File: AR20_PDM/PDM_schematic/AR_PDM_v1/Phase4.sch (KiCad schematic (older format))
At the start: 10 parts, among them Q7 BTS50025-1TAD, U7 INA233

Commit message: Working on pcb layout
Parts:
- removed D?: D_Schottky_x2, symbol AR20_PDM_v1-rescue:D_Schottky_x2
- added D53, D54: D_Schottky_BAT60A, AR_PDM_v1:D_Shotky_BAT60_HandSoldering, symbol AR20_PDM_v1-rescue:D_Schottky_BAT60A
- gave numbers to parts that had none: 4
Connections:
- net GND: now also D53.2 (A), D54.2 (A)
- net at R117.1, U7.10 (IN+): now also D54.1 (K)
- net at R115.1, U7.9 (In-): now also D53.1 (K)
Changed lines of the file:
@@
 AR Path="/5E0FB5C8/5EE91E06" Ref="R?"  Part="1"
 AR Path="/5E0FBBBD/5EE91E06" Ref="R?"  Part="1"
-AR Path="/5E0FC3A2/5EE91E06" Ref="R?"  Part="1"
+AR Path="/5E0FC3A2/5EE91E06" Ref="R116"  Part="1"
 AR Path="/5E0FCFDC/5EE91E06" Ref="R?"  Part="1"
 AR Path="/5E0FDCCC/5EE91E06" Ref="R?"  Part="1"
 AR Path="/5E10174B/5EE91E06" Ref="R?"  Part="1"
-F 0 "R?" V 6643 1600 50  0000 C CNN
+F 0 "R116" V 6643 1600 50  0000 C CNN
 F 1 "2m_1%_4W" V 6734 1600 50  0000 C CNN
 F 2 "Resistor_SMD:R_2512_6332Metric" V 6780 1600 50  0001 C CNN
@@
 Text HLabel 7300 1600 2    50   Input ~ 10
 V+12V
-$Comp
-L AR20_PDM_v1-rescue:D_Schottky_x2 D?
-U 1 1 5EE91E0D
-P 6950 4825
-AR Path="/5DA89415/5EE91E0D" Ref="D?"  Part="1"
-AR Path="/5E0FC3A2/5EE91E0D" Ref="D?"  Part="1"
-F 0 "D?" H 6950 5041 50  0000 C CNN
-F 1 "D_Schottky_x2" H 6950 4950 50  0000 C CNN
-F 2 "" H 6950 4825 50  0001 C CNN
-F 3 "~" H 6950 4825 50  0001 C CNN
-	1    6950 4825
-	1    0    0    -1
-$EndComp
 $Comp
 L AR20_PDM_v1-rescue:R-Device R?
@@
 AR Path="/5E0FB5C8/5EE91E13" Ref="R?"  Part="1"
 AR Path="/5E0FBBBD/5EE91E13" Ref="R?"  Part="1"
-AR Path="/5E0FC3A2/5EE91E13" Ref="R?"  Part="1"
+AR Path="/5E0FC3A2/5EE91E13" Ref="R115"  Part="1"
 AR Path="/5E0FCFDC/5EE91E13" Ref="R?"  Part="1"
 AR Path="/5E0FDCCC/5EE91E13" Ref="R?"  Part="1"
 AR Path="/5E10174B/5EE91E13" Ref="R?"  Part="1"
-F 0 "R?" V 6443 3850 50  0000 C CNN
+F 0 "R115" V 6443 3850 50  0000 C CNN
 F 1 "1K_1%" V 6534 3850 50  0000 C CNN
 F 2 "Resistor_SMD:R_0603_1608Metric" V 6580 3850 50  0001 C CNN
@@
 AR Path="/5E0FB5C8/5EE91E19" Ref="R?"  Part="1"
 AR Path="/5E0FBBBD/5EE91E19" Ref="R?"  Part="1"
-AR Path="/5E0FC3A2/5EE91E19" Ref="R?"  Part="1"
+AR Path="/5E0FC3A2/5EE91E19" Ref="R117"  Part="1"
 AR Path="/5E0FCFDC/5EE91E19" Ref="R?"  Part="1"
 AR Path="/5E0FDCCC/5EE91E19" Ref="R?"  Part="1"
 AR Path="/5E10174B/5EE91E19" Ref="R?"  Part="1"
-F 0 "R?" V 6843 3850 50  0000 C CNN
+F 0 "R117" V 6843 3850 50  0000 C CNN
 F 1 "1K_1%" V 6934 3850 50  0000 C CNN
 F 2 "Resistor_SMD:R_0603_1608Metric" V 6980 3850 50  0001 C CNN
@@
 Text Notes 7075 2000 0    50   ~ 10
 Place shunt and INA233 close, \nroute togethere, differentialy pair. \nKeep short, and away from Noise.
-$Comp
-L AR20_PDM_v1-rescue:GND-power #PWR?
-U 1 1 5EE91E27
-P 6950 5025
-AR Path="/5DA89415/5EE91E27" Ref="#PWR?"  Part="1"
-AR Path="/5DEB10A1/5EE91E27" Ref="#PWR?"  Part="1"
-AR Path="/5DEB20EA/5EE91E27" Ref="#PWR?"  Part="1"
-AR Path="/5E0E4725/5EE91E27" Ref="#PWR?"  Part="1"
-AR Path="/5E0E4A93/5EE91E27" Ref="#PWR?"  Part="1"
-AR Path="/5E0E4EB5/5EE91E27" Ref="#PWR?"  Part="1"
-AR Path="/5E0E5304/5EE91E27" Ref="#PWR?"  Part="1"
-AR Path="/5E0E594B/5EE91E27" Ref="#PWR?"  Part="1"
-AR Path="/5E0E607C/5EE91E27" Ref="#PWR?"  Part="1"
-AR Path="/5E0FB5C8/5EE91E27" Ref="#PWR?"  Part="1"
-AR Path="/5E0FBBBD/5EE91E27" Ref="#PWR?"  Part="1"
-AR Path="/5E0FC3A2/5EE91E27" Ref="#PWR?"  Part="1"
-AR Path="/5E0FCFDC/5EE91E27" Ref="#PWR?"  Part="1"
-AR Path="/5E0FDCCC/5EE91E27" Ref="#PWR?"  Part="1"
-AR Path="/5E10174B/5EE91E27" Ref="#PWR?"  Part="1"
-F 0 "#PWR?" H 6950 4775 50  0001 C CNN
-F 1 "GND" H 6955 4852 50  0000 C CNN
-F 2 "" H 6950 5025 50  0001 C CNN
-F 3 "" H 6950 5025 50  0001 C CNN
-	1    6950 5025
-	1    0    0    -1
-$EndComp
 Wire Wire Line
 	4775 1600 6650 1600
@@
 Wire Wire Line
 	6650 4400 8750 4400
-Connection ~ 6650 4400
-Wire Wire Line
-	6650 4400 6650 4825
-Wire Wire Line
-	8750 4300 7250 4300
-Wire Wire Line
-	7250 4825 7250 4300
-Connection ~ 7250 4300
-Wire Wire Line
-	7250 4300 7050 4300
 $Comp
 L AR20_PDM_v1-rescue:R-Device R?
@@
 AR Path="/5E0FB5C8/5EEC4799" Ref="R?"  Part="1"
 AR Path="/5E0FBBBD/5EEC4799" Ref="R?"  Part="1"
-AR Path="/5E0FC3A2/5EEC4799" Ref="R?"  Part="1"
+AR Path="/5E0FC3A2/5EEC4799" Ref="R118"  Part="1"
 AR Path="/5E0FCFDC/5EEC4799" Ref="R?"  Part="1"
 AR Path="/5E0FDCCC/5EEC4799" Ref="R?"  Part="1"
 AR Path="/5E10174B/5EEC4799" Ref="R?"  Part="1"
-F 0 "R?" V 8093 4100 50  0000 C CNN
+F 0 "R118" V 8093 4100 50  0000 C CNN
 F 1 "10K" V 8184 4100 50  0000 C CNN
 F 2 "Resistor_SMD:R_0603_1608Metric" V 8230 4100 50  0001 C CNN
@@
 Text HLabel 8150 4100 0    50   Output ~ 10
 P4_OUT
+Wire Wire Line
+	7050 4300 7100 4300
+$Comp
+L AR20_PDM_v1-rescue:D_Schottky_BAT60A D?
+U 1 1 5EFA8D57
+P 6700 4775
+AR Path="/5DA89415/5EFA8D57" Ref="D?"  Part="1"
+AR Path="/5E0FC3A2/5EFA8D57" Ref="D53"  Part="1"
+F 0 "D53" V 6530 4885 50  0000 L CNN
+F 1 "D_Schottky_BAT60A" V 6621 4885 50  0000 L CNN
+F 2 "AR_PDM_v1:D_Shotky_BAT60_HandSoldering" H 6800 4725 50  0001 C CNN
+F 3 "~" H 6800 4725 50  0001 C CNN
+	1    6700 4775
+	0    1    1    0
+$EndComp
+$Comp
+L AR20_PDM_v1-rescue:GND-power #PWR?
+U 1 1 5EFA8D5D
+P 6875 4950
+AR Path="/5DA89415/5EFA8D5D" Ref="#PWR?"  Part="1"
+AR Path="/5DEB10A1/5EFA8D5D" Ref="#PWR?"  Part="1"
+AR Path="/5DEB20EA/5EFA8D5D" Ref="#PWR?"  Part="1"
+AR Path="/5E0E4725/5EFA8D5D" Ref="#PWR?"  Part="1"
+AR Path="/5E0E4A93/5EFA8D5D" Ref="#PWR?"  Part="1"
+AR Path="/5E0E4EB5/5EFA8D5D" Ref="#PWR?"  Part="1"
+AR Path="/5E0E5304/5EFA8D5D" Ref="#PWR?"  Part="1"
+AR Path="/5E0E594B/5EFA8D5D" Ref="#PWR?"  Part="1"
+AR Path="/5E0E607C/5EFA8D5D" Ref="#PWR?"  Part="1"
+AR Path="/5E0FB5C8/5EFA8D5D" Ref="#PWR?"  Part="1"
+AR Path="/5E0FBBBD/5EFA8D5D" Ref="#PWR?"  Part="1"
+AR Path="/5E0FC3A2/5EFA8D5D" Ref="#PWR022"  Part="1"
+AR Path="/5E0FCFDC/5EFA8D5D" Ref="#PWR?"  Part="1"
+AR Path="/5E0FDCCC/5EFA8D5D" Ref="#PWR?"  Part="1"
+AR Path="/5E10174B/5EFA8D5D" Ref="#PWR?"  Part="1"
+F 0 "#PWR022" H 6875 4700 50  0001 C CNN
+F 1 "GND" H 6880 4777 50  0000 C CNN
+F 2 "" H 6875 4950 50  0001 C CNN
+F 3 "" H 6875 4950 50  0001 C CNN
+	1    6875 4950
+	1    0    0    -1
+$EndComp
+$Comp
+L AR20_PDM_v1-rescue:D_Schottky_BAT60A D?
+U 1 1 5EFA8D63
+P 7150 4775
+AR Path="/5DA89415/5EFA8D63" Ref="D?"  Part="1"
+AR Path="/5E0FC3A2/5EFA8D63" Ref="D54"  Part="1"
+F 0 "D54" V 6980 4885 50  0000 L CNN
+F 1 "D_Schottky_BAT60A" V 7071 4885 50  0000 L CNN
+F 2 "AR_PDM_v1:D_Shotky_BAT60_HandSoldering" H 7250 4725 50  0001 C CNN
+F 3 "~" H 7250 4725 50  0001 C CNN
+	1    7150 4775
+	0    1    1    0
+$EndComp
+Wire Wire Line
+	6650 4475 6650 4400
+Wire Wire Line
+	7100 4475 7100 4300
+Wire Wire Line
+	6650 4825 6875 4825
+Wire Wire Line
+	6875 4950 6875 4825
+Connection ~ 6875 4825
+Wire Wire Line
+	6875 4825 7100 4825
+Connection ~ 7100 4300
+Wire Wire Line
+	7100 4300 8750 4300
+Connection ~ 6650 4400
 $EndSCHEMATC

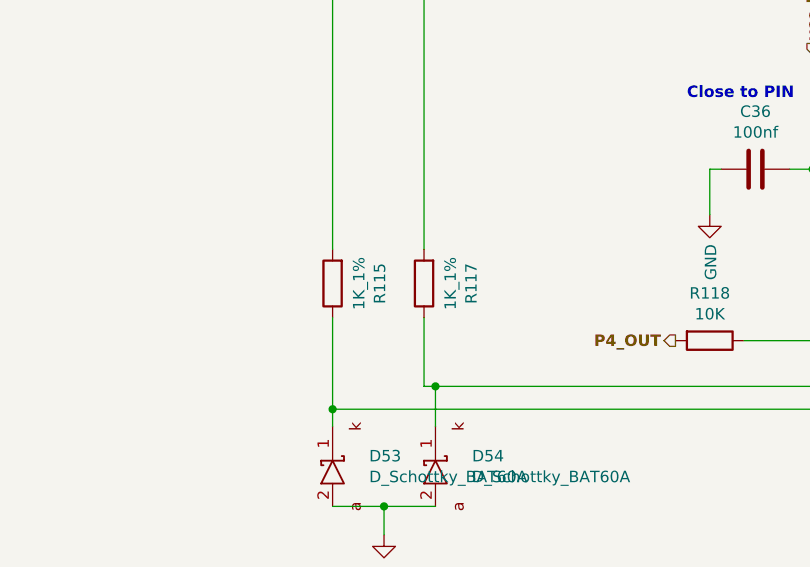
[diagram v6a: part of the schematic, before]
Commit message: shematics adjustments, and fixing values and names
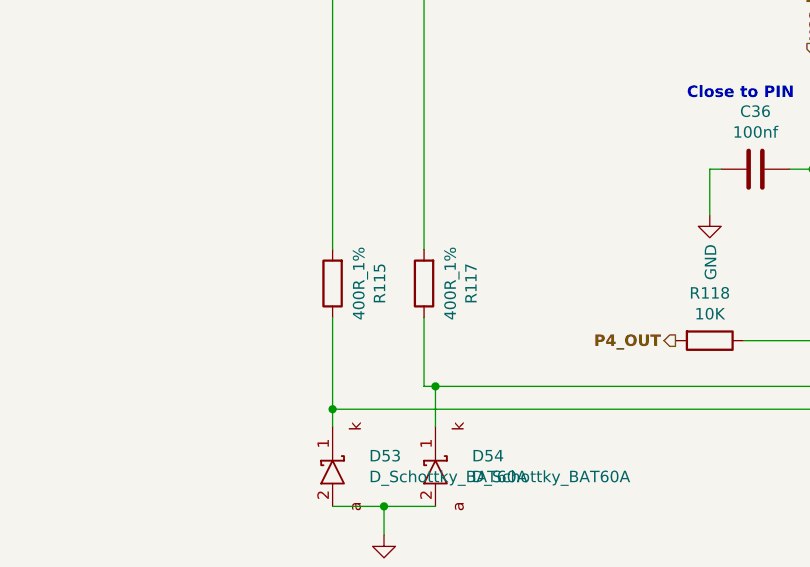
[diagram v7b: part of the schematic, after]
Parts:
- R115, R117: value 1K_1% -> 400R_1%
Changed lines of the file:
@@
 AR Path="/5E10174B/5EE91E13" Ref="R?"  Part="1"
 F 0 "R115" V 6443 3850 50  0000 C CNN
-F 1 "1K_1%" V 6534 3850 50  0000 C CNN
+F 1 "400R_1%" V 6534 3850 50  0000 C CNN
 F 2 "Resistor_SMD:R_0603_1608Metric" V 6580 3850 50  0001 C CNN
 F 3 "~" H 6650 3850 50  0001 C CNN
@@
 AR Path="/5E10174B/5EE91E19" Ref="R?"  Part="1"
 F 0 "R117" V 6843 3850 50  0000 C CNN
-F 1 "1K_1%" V 6934 3850 50  0000 C CNN
+F 1 "400R_1%" V 6934 3850 50  0000 C CNN
 F 2 "Resistor_SMD:R_0603_1608Metric" V 6980 3850 50  0001 C CNN
 F 3 "~" H 7050 3850 50  0001 C CNN
